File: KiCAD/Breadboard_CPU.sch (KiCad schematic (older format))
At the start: 21 parts, among them Q101 2N2222, SW101 RST

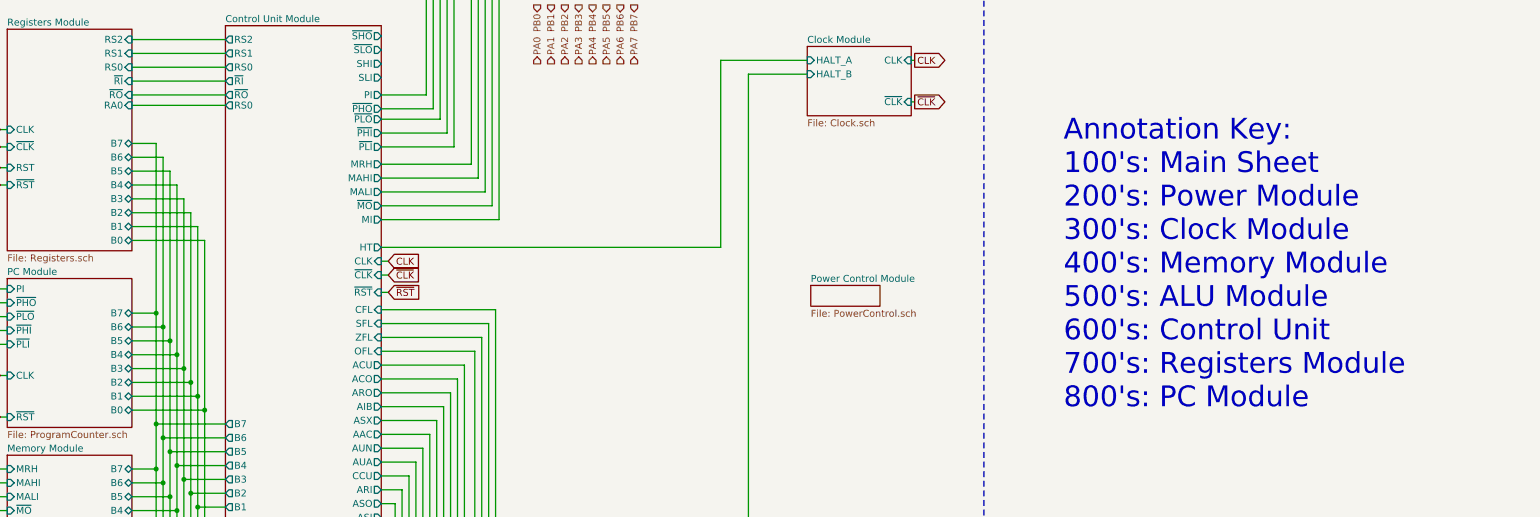
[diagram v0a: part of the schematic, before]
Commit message: Moved SP out of register module into SP module; changed RS0 assert signal alias from RS0 to RSH; moved uCode and program code to different subdirs of Programming/ .
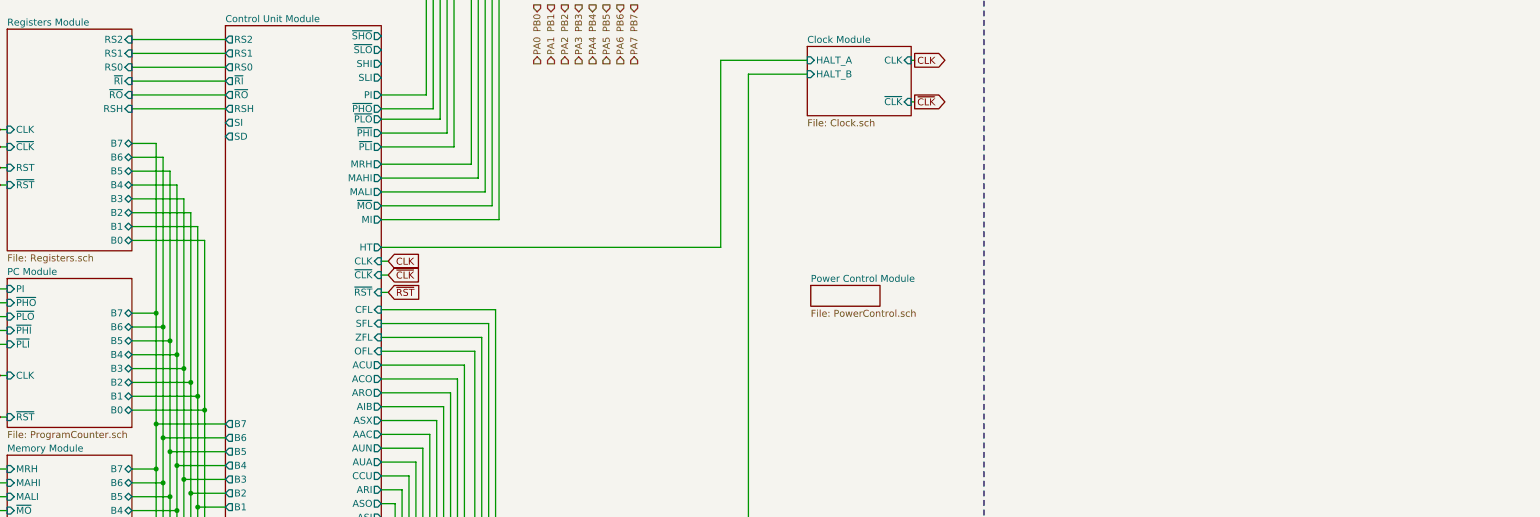
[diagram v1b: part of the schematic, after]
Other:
- note removed: "Annotation Key:\n100's: Main Sheet\n200's: Power Module\n300's: Clock Module\n400's: Memory Module\n500's: ALU Module\n600's: Control Unit\n700's: Registers Module\n800's: PC Module"
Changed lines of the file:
@@
 F5 "HALT_B" I L 9075 3075 50
 $EndSheet
-Text Notes 10925 5500 0    150  ~ 0
-Annotation Key:\n100's: Main Sheet\n200's: Power Module\n300's: Clock Module\n400's: Memory Module\n500's: ALU Module\n600's: Control Unit\n700's: Registers Module\n800's: PC Module
 $Sheet
 S 3300 5825 900  975
@@
 F15 "~RST" I L 3300 3875 50
 F16 "RST" I L 3300 3750 50
-F17 "RA0" I R 4200 3300 50
-F18 "CLK" I L 3300 3475 50
-F19 "~CLK" I L 3300 3600 50
+F17 "CLK" I L 3300 3475 50
+F18 "~CLK" I L 3300 3600 50
+F19 "RSH" I R 4200 3325 50
 $EndSheet
 Wire Wire Line
@@
 	4725 4275 4725 5500
 Wire Wire Line
-	4200 3300 4875 3300
+	4200 3325 4875 3325
 Text GLabel 3250 3475 0    50   Input ~ 0
 CLK
@@
 F35 "HT" O R 6000 4325 50
 F36 "CFL" I R 6000 4775 50
-F37 "RS0" O L 4875 3300 50
-F38 "PI" O R 6000 3225 50
-F39 "MALI" O R 6000 3925 50
-F40 "MAHI" O R 6000 3825 50
-F41 "~PHO" O R 6000 3325 50
-F42 "~PLO" O R 6000 3400 50
-F43 "SLI" O R 6000 3100 50
-F44 "SHI" O R 6000 3000 50
-F45 "~SLO" O R 6000 2900 50
-F46 "~SHO" O R 6000 2800 50
-F47 "~PHI" O R 6000 3500 50
-F48 "~PLI" O R 6000 3600 50
-F49 "MRH" O R 6000 3725 50
+F37 "PI" O R 6000 3225 50
+F38 "MALI" O R 6000 3925 50
+F39 "MAHI" O R 6000 3825 50
+F40 "~PHO" O R 6000 3325 50
+F41 "~PLO" O R 6000 3400 50
+F42 "SLI" O R 6000 3100 50
+F43 "SHI" O R 6000 3000 50
+F44 "~SLO" O R 6000 2900 50
+F45 "~SHO" O R 6000 2800 50
+F46 "~PHI" O R 6000 3500 50
+F47 "~PLI" O R 6000 3600 50
+F48 "MRH" O R 6000 3725 50
+F49 "SI" O L 4875 3425 50
+F50 "SD" O L 4875 3525 50
+F51 "RSH" O L 4875 3325 50
 $EndSheet
 Wire Wire Line

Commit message: First working versiongit add .  Added CSU control signal for updating C and O flags during add operations only.  Added circuitry to disable the reg decoder unless ~RI or ~RO are asserted.  Potential future issues: PC clock noise, reg clock noise, clock module being crap..
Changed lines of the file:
@@
 F26 "ACU" I R 6000 7825 50
 F27 "CFL" O R 6000 8225 50
+F28 "CSU_CLK" I L 4875 8300 50
 $EndSheet
 Connection ~ 4375 6700
@@
 F50 "SD" O L 4875 3525 50
 F51 "RSH" O L 4875 3325 50
+F52 "CSU_CLK" O L 4875 5025 50
 $EndSheet
 Wire Wire Line
